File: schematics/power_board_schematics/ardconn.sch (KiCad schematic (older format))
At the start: 1 part, among them J7 CONN_01X16

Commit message: Added more connections
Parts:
- added J8: Conn_01x08_Male, symbol Connector:Conn_01x08_Male
- added U1: Conn_0_to_7, symbol custom:Conn_0_to_7
- added U2: conn_8_to_13, symbol custom:conn_8_to_13
- added U3: Conn_14_to_21, symbol custom:Conn_14_to_21
- added U4: conn_A8_to_A15, symbol custom:conn_A8_to_A15
- added U5: conn_A0_to_A7, symbol custom:conn_A0_to_A7
- added U6: conn_22_to_53, symbol custom:conn_22_to_53
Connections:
- new net Ignition_Primary_Power: U6.28 (Pin_28)
- new net Ignition_Primary_Select: U6.29 (Pin_31)
- new net Ignition_Secondary_Power: U6.37 (Pin_16)
- new net Ignition_Secondary_Select: U6.36 (Pin_36)
- new net Limitsw_Linac_EXT: U6.31 (Pin_31)
- new net Limitsw_Linac_Ret: U6.30 (Pin_30)
- new net Limitsw_Remotefill_CLS: U6.35 (Pin_14)
- new net Limitsw_Remotefill_OPN: U6.34 (Pin_34)
- new net Limitsw_Remotevent_OPN: U6.33 (Pin_12)
- new net Limitsw_Removevent_CLS: U6.32 (Pin_32)
- new net Linactuator_Power: U6.22 (Pin_22)
- new net Linactuator_Select: U6.23 (Pin_31)
- new net Remotefill_Power: U6.26 (Pin_26)
- new net Remotefill_Select: U6.27 (Pin_31)
- new net Remotevent_Power: U6.25 (Pin_31)
- new net Remotevent_Select: U6.24 (Pin_24)
- new net SD_SS: U6.53 (Pin_32)
- new net Sevenseg_A: U6.39 (Pin_18)
- new net Sevenseg_B: U6.40 (Pin_40)
- new net Sevenseg_C: U6.43 (Pin_22)
- new net Sevenseg_D: U6.45 (Pin_24)
- new net Sevenseg_D1: U6.47 (Pin_26)
- new net Sevenseg_D2: U6.46 (Pin_46)
- new net Sevenseg_DP: U6.44 (Pin_44)
- new net Sevenseg_E: U6.42 (Pin_42)
- new net Sevenseg_F: U6.41 (Pin_20)
- new net Sevenseg_G: U6.38 (Pin_38)
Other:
- note added: "Arduino Pins 14 - 21"
- note added: "Arduino Pins 22 - 53"
- note added: "Arduino Pins 8 - 13 \n+ some others\n"
- note added: "Arduino Pins A0 - A7"
- note added: "Arduino Pins A8 - A15"
- note added: "Arduino Pins Power"
- note added: "Arudino Pins 0 - 7"
- moved on the sheet: J7

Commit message: First commit
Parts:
- removed J8: Conn_01x08_Male, symbol Connector:Conn_01x08_Male
- added Button: SW_Push, symbol Switch:SW_Push
- added U?: conn_power, symbol custom:conn_power
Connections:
- net GND: now reaches U6.56 (Pin_56)
- net GND: now also U6.57 (Pin_57)
- net Ignition_Primary_Power: no longer names the net of U6.28 (Pin_28)
- net Ignition_Primary_Select: no longer names the net of U6.29 (Pin_31)
- net Ignition_Secondary_Power: no longer names the net of U6.37 (Pin_16)
- net Ignition_Secondary_Select: no longer names the net of U6.36 (Pin_36)
- net Limitsw_Linac_EXT: no longer names the net of U6.31 (Pin_31)
- net Limitsw_Linac_Ret: no longer names the net of U6.30 (Pin_30)
- net Limitsw_Remotefill_CLS: no longer names the net of U6.35 (Pin_14)
- net Limitsw_Remotefill_OPN: no longer names the net of U6.34 (Pin_34)
- net Limitsw_Remotevent_OPN: no longer names the net of U6.33 (Pin_12)
- net Limitsw_Removevent_CLS: no longer names the net of U6.32 (Pin_32)
- net Remotefill_Power: no longer names the net of U6.26 (Pin_26)
- net Remotefill_Select: no longer names the net of U6.27 (Pin_31)
- net Remotevent_Power: no longer names the net of U6.25 (Pin_31)
- net Remotevent_Select: no longer names the net of U6.24 (Pin_24)
- new net: Button.1, U?.2 (RESET)
- new net: Button.2, U?.5 (GND)
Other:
- moved on the sheet: U2

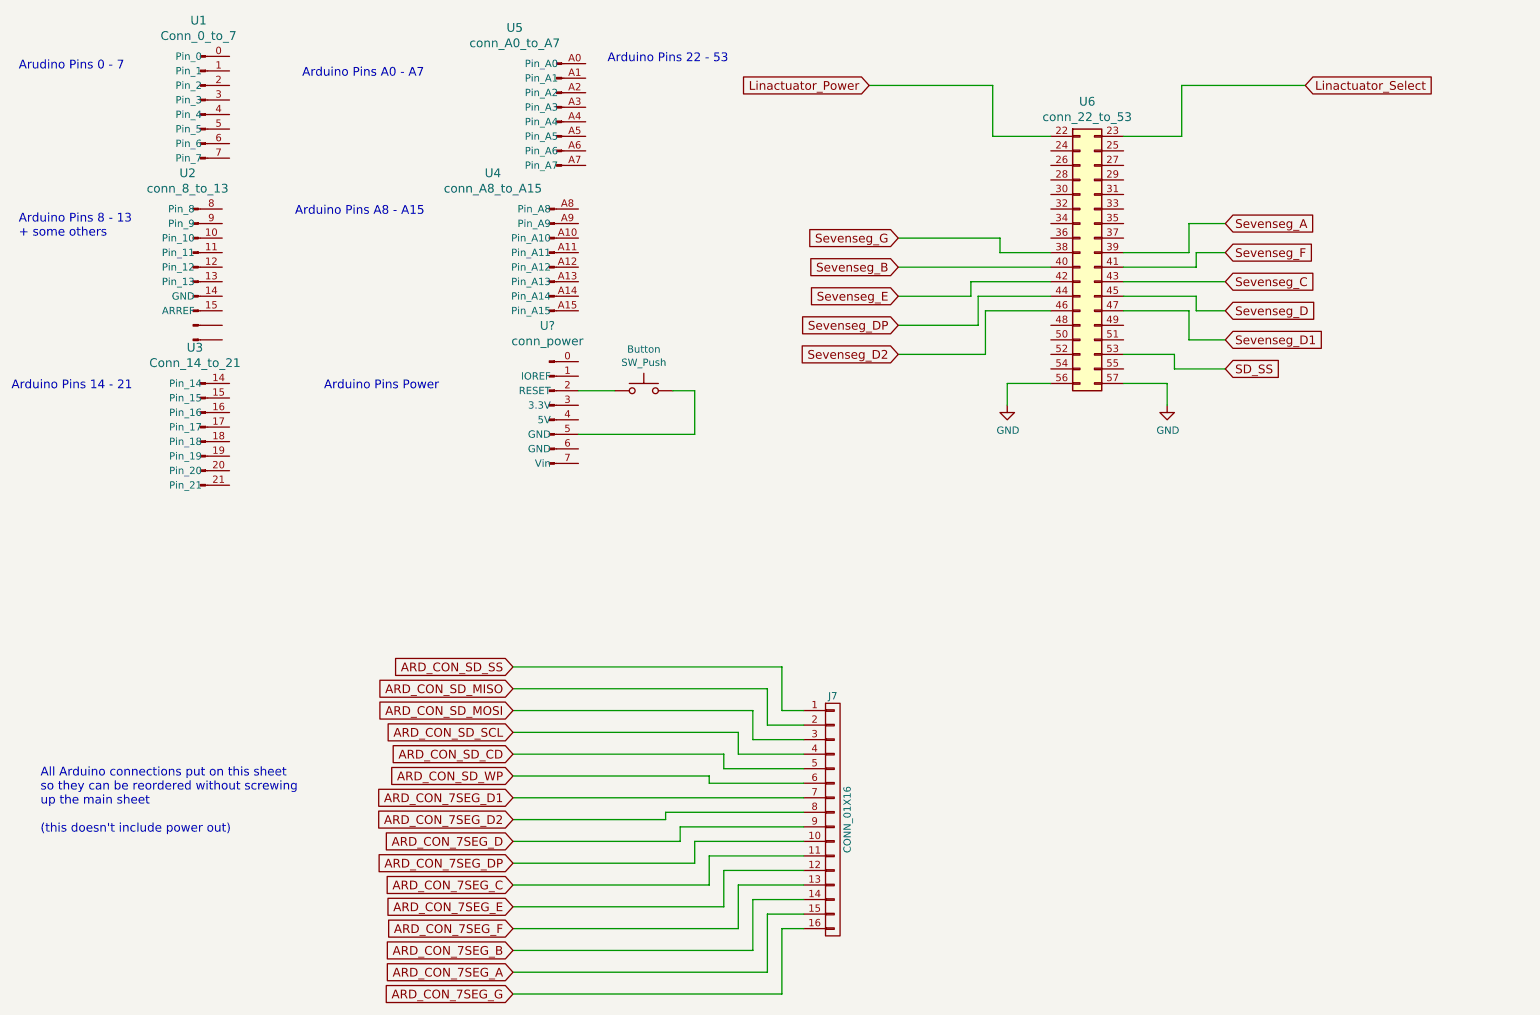
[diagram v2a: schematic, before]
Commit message: Set CD and WP to 54 and 55 respectively
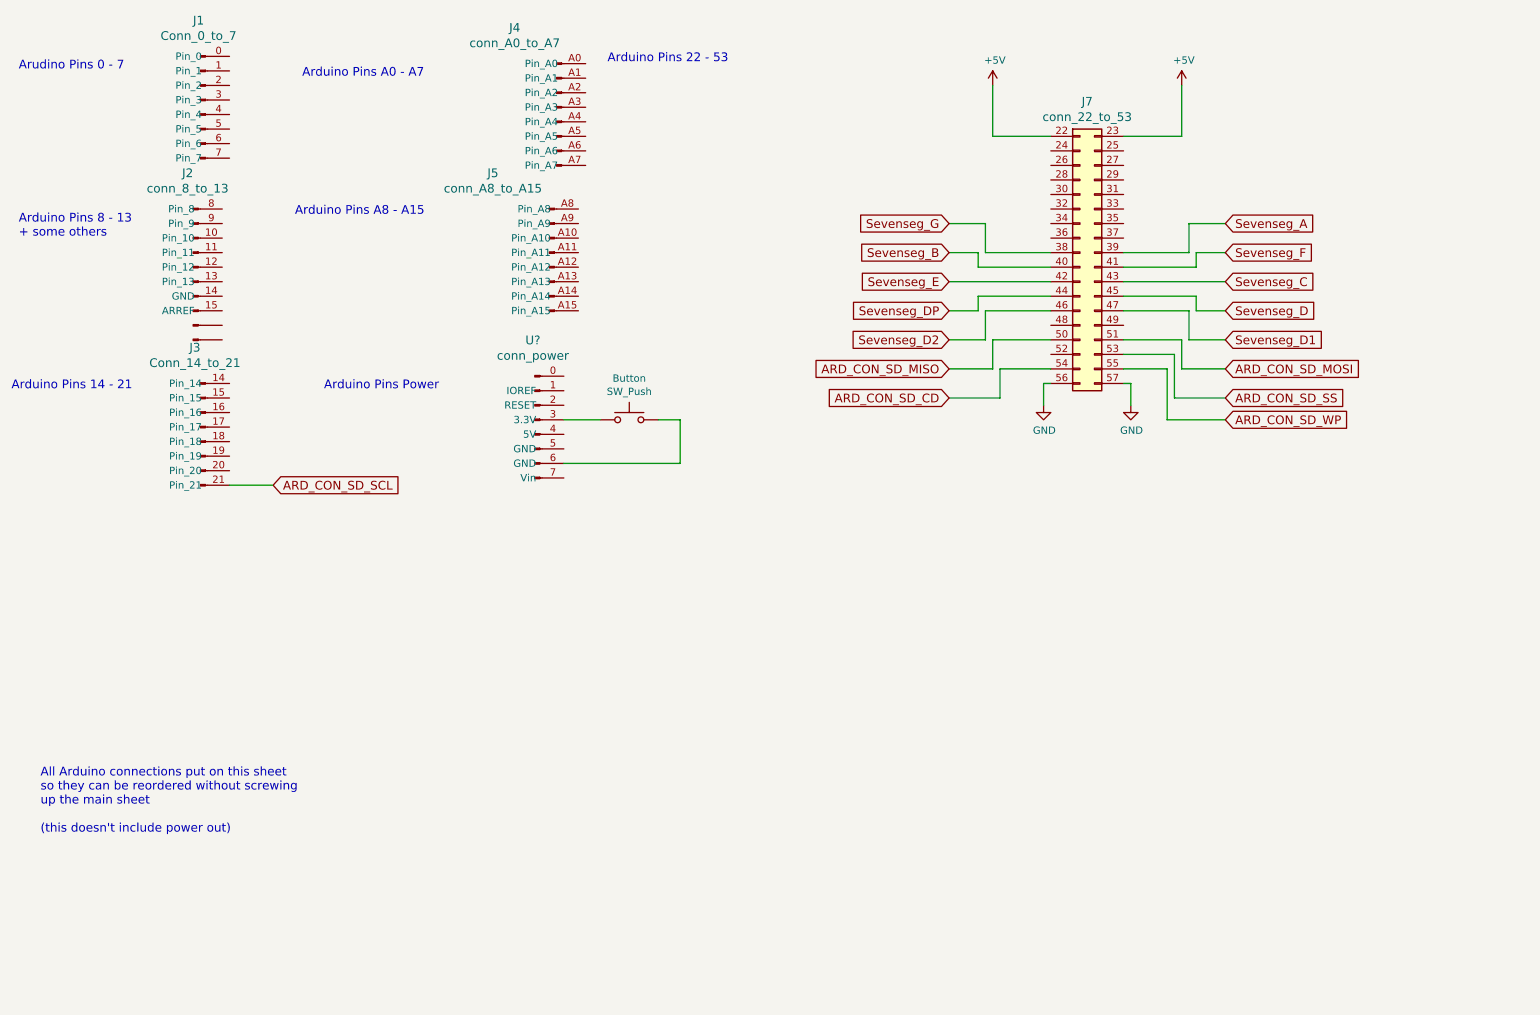
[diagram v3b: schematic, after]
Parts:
- removed J7: CONN_01X16, Pin_Headers:Pin_Header_Straight_2x08_Pitch2.54mm, symbol rlcs_power-rescue:CONN_01X16
- removed U?: conn_power, symbol custom:conn_power
- added U?: conn_power, symbol custom:conn_power
- renumbered U1 to J1, U2 to J2, U3 to J3, U5 to J4, U4 to J5, U6 to J7
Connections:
- net Linactuator_Select is gone; now on net +5V: J7.23 (Pin_31)
- net SD_SS is gone; now on net ARD_CON_SD_SS: J7.53 (Pin_32)
- net ARD_CON_SD_CD: now also J7.54 (Pin_54)
- net ARD_CON_SD_MISO: now also J7.50 (Pin_50)
- net ARD_CON_SD_MOSI: now also J7.51 (Pin_30)
- net ARD_CON_SD_SCL: now also J3.21 (Pin_21)
- net ARD_CON_SD_WP: now also J7.55 (Pin_55)
- net at Button.1: now also U?.3 (3.3V)
- net at Button.2: now also U?.6 (GND)
- net Linactuator_Power renamed +5V
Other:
- moved on the sheet: Button

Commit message: third commit, mainly made it more consistent
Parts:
- gave numbers to parts that had none: 1
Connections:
- net at Button.1: now also J6.2 (RESET); no longer J6.3 (3.3V)
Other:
- moved on the sheet: Button
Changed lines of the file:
@@
 L Switch:SW_Push Button
 U 1 1 5EB5D71A
-P 4900 3350
-F 0 "Button" H 4900 3635 50  0000 C CNN
-F 1 "SW_Push" H 4900 3544 50  0000 C CNN
-F 2 "" H 4900 3550 50  0001 C CNN
-F 3 "~" H 4900 3550 50  0001 C CNN
-	1    4900 3350
+P 4900 3250
+F 0 "Button" H 4900 3535 50  0000 C CNN
+F 1 "SW_Push" H 4900 3444 50  0000 C CNN
+F 2 "" H 4900 3450 50  0001 C CNN
+F 3 "~" H 4900 3450 50  0001 C CNN
+	1    4900 3250
 	1    0    0    -1
 $EndComp
@@
 	5250 3650 4450 3650
 Wire Wire Line
-	4700 3350 4450 3350
+	4700 3250 4450 3250
 Text GLabel 9000 2200 2    60   Input ~ 0
 Sevenseg_F
@@
 Sevenseg_DP
 Wire Wire Line
-	5250 3350 5250 3650
-Wire Wire Line
-	5100 3350 5250 3350
+	5100 3250 5250 3250
 Wire Wire Line
 	8750 2800 9000 2800
@@
 	8600 3000 8300 3000
 $Comp
-L custom:conn_power U?
+L custom:conn_power J6
 U 1 1 5ED49DCC
 P 4350 3000
-F 0 "U?" H 4237 3197 60  0000 C CNN
+F 0 "J6" H 4237 3197 60  0000 C CNN
 F 1 "conn_power" H 4237 3091 60  0000 C CNN
 F 2 "" H 4350 3200 60  0001 C CNN
@@
 	1    0    0    -1
 $EndComp
+Wire Wire Line
+	5250 3250 5250 3650
 $EndSCHEMATC

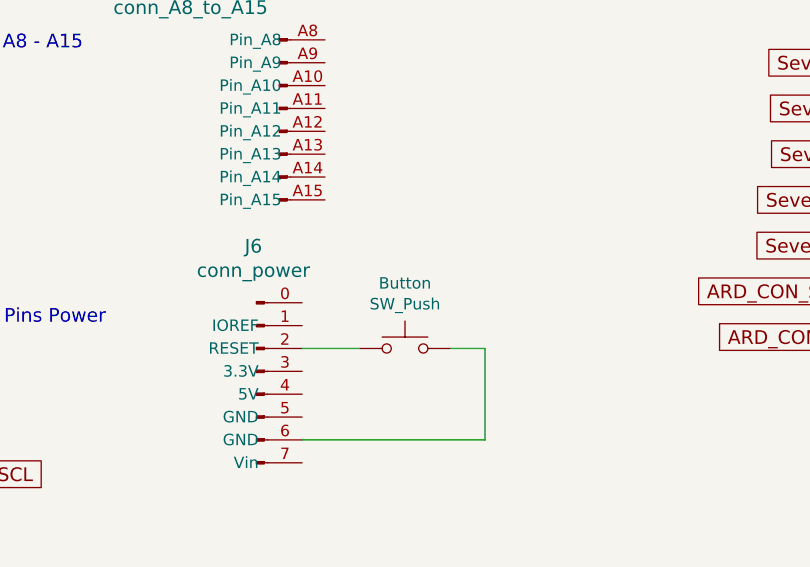
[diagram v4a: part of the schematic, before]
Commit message: Fixed the reference designators
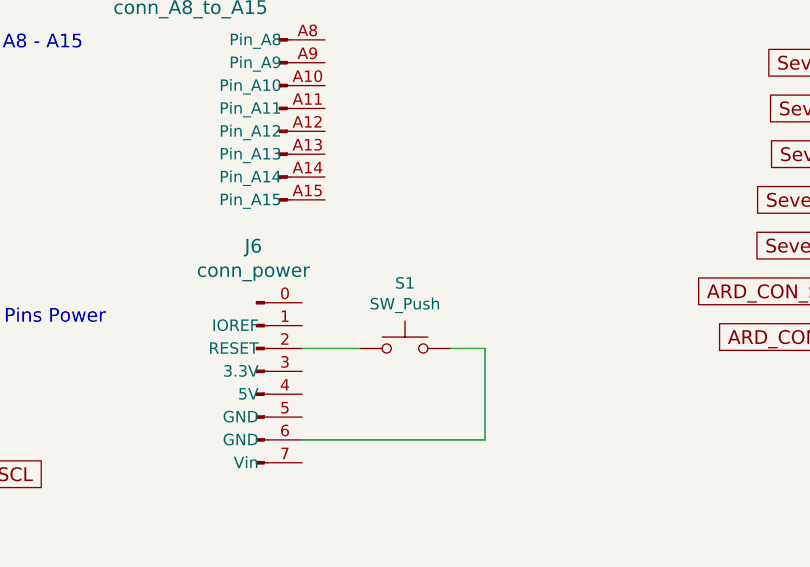
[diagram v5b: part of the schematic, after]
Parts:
- renumbered Button to S1
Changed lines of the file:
@@
 	8700 1400 8700 1050
 $Comp
-L Switch:SW_Push Button
+L Switch:SW_Push S1
 U 1 1 5EB5D71A
 P 4900 3250
-F 0 "Button" H 4900 3535 50  0000 C CNN
+F 0 "S1" H 4900 3535 50  0000 C CNN
 F 1 "SW_Push" H 4900 3444 50  0000 C CNN
 F 2 "" H 4900 3450 50  0001 C CNN

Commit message: Made the pcb
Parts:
- J10: renamed from J3; footprint (none) -> Connector_PinSocket_2.54mm:PinSocket_1x08_P2.54mm_Vertical
- J11: renamed from J6; footprint (none) -> Connector_PinSocket_2.54mm:PinSocket_1x08_P2.54mm_Vertical
- J12: renamed from J5; footprint (none) -> Connector_PinSocket_2.54mm:PinSocket_1x08_P2.54mm_Vertical
- J13: renamed from J4; footprint (none) -> Connector_PinSocket_2.54mm:PinSocket_1x08_P2.54mm_Vertical
- J14: renamed from J7; footprint (none) -> Connector_PinSocket_2.54mm:PinSocket_2x18_P2.54mm_Vertical
- J8: renamed from J1; footprint (none) -> Connector_PinSocket_2.54mm:PinSocket_1x08_P2.54mm_Vertical
- J9: renamed from J2; footprint (none) -> Connector_PinHeader_2.54mm:PinHeader_1x10_P2.54mm_Vertical
- S1: footprint (none) -> Button_Switch_SMD:SW_DIP_SPSTx01_Slide_9.78x4.72mm_W8.61mm_P2.54mm
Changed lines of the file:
@@
 ARD_CON_SD_SCL
 $Comp
-L custom:conn_22_to_53 J7
+L custom:conn_22_to_53 J14
 U 1 1 5E7AFC08
 P 8050 2200
-F 0 "J7" H 8050 3239 60  0000 C CNN
+F 0 "J14" H 8050 3239 60  0000 C CNN
 F 1 "conn_22_to_53" H 8050 3133 60  0000 C CNN
-F 2 "" H 8000 3250 60  0001 C CNN
+F 2 "Connector_PinSocket_2.54mm:PinSocket_2x18_P2.54mm_Vertical" H 8000 3250 60  0001 C CNN
 F 3 "" H 8000 3250 60  0001 C CNN
 	1    8050 2200
@@
 $EndComp
 $Comp
-L custom:Conn_0_to_7 J1
+L custom:Conn_0_to_7 J8
 U 1 1 5E7B26E9
 P 2000 1100
-F 0 "J1" H 1937 1597 60  0000 C CNN
+F 0 "J8" H 1937 1597 60  0000 C CNN
 F 1 "Conn_0_to_7" H 1937 1491 60  0000 C CNN
-F 2 "" H 1900 1800 60  0001 C CNN
+F 2 "Connector_PinSocket_2.54mm:PinSocket_1x08_P2.54mm_Vertical" H 1900 1800 60  0001 C CNN
 F 3 "" H 1900 1800 60  0001 C CNN
 	1    2000 1100
@@
 $EndComp
 $Comp
-L custom:conn_8_to_13 J2
+L custom:conn_8_to_13 J9
 U 1 1 5E7B5F51
 P 2000 2250
-F 0 "J2" H 1862 2847 60  0000 C CNN
+F 0 "J9" H 1862 2847 60  0000 C CNN
 F 1 "conn_8_to_13" H 1862 2741 60  0000 C CNN
-F 2 "" H 2000 3150 60  0001 C CNN
+F 2 "Connector_PinHeader_2.54mm:PinHeader_1x10_P2.54mm_Vertical" H 2000 3150 60  0001 C CNN
 F 3 "" H 2000 3150 60  0001 C CNN
 	1    2000 2250
@@
 $EndComp
 $Comp
-L custom:Conn_14_to_21 J3
+L custom:Conn_14_to_21 J10
 U 1 1 5E7B8C25
 P 2050 3350
-F 0 "J3" H 1912 3847 60  0000 C CNN
+F 0 "J10" H 1912 3847 60  0000 C CNN
 F 1 "Conn_14_to_21" H 1912 3741 60  0000 C CNN
-F 2 "" H 1950 4250 60  0001 C CNN
+F 2 "Connector_PinSocket_2.54mm:PinSocket_1x08_P2.54mm_Vertical" H 1950 4250 60  0001 C CNN
 F 3 "" H 1950 4250 60  0001 C CNN
 	1    2050 3350
@@
 $EndComp
 $Comp
-L custom:conn_A0_to_A7 J4
+L custom:conn_A0_to_A7 J13
 U 1 1 5E7C0D80
 P 4500 1250
-F 0 "J4" H 4112 1847 60  0000 C CNN
+F 0 "J13" H 4112 1847 60  0000 C CNN
 F 1 "conn_A0_to_A7" H 4112 1741 60  0000 C CNN
-F 2 "" H 4500 1850 60  0001 C CNN
+F 2 "Connector_PinSocket_2.54mm:PinSocket_1x08_P2.54mm_Vertical" H 4500 1850 60  0001 C CNN
 F 3 "" H 4500 1850 60  0001 C CNN
 	1    4500 1250
@@
 $EndComp
 $Comp
-L custom:conn_A8_to_A15 J5
+L custom:conn_A8_to_A15 J12
 U 1 1 5E7C1AAF
 P 4400 2250
-F 0 "J5" H 3962 2847 60  0000 C CNN
+F 0 "J12" H 3962 2847 60  0000 C CNN
 F 1 "conn_A8_to_A15" H 3962 2741 60  0000 C CNN
-F 2 "" H 4450 2850 60  0001 C CNN
+F 2 "Connector_PinSocket_2.54mm:PinSocket_1x08_P2.54mm_Vertical" H 4450 2850 60  0001 C CNN
 F 3 "" H 4450 2850 60  0001 C CNN
 	1    4400 2250
@@
 F 0 "S1" H 4900 3535 50  0000 C CNN
 F 1 "SW_Push" H 4900 3444 50  0000 C CNN
-F 2 "" H 4900 3450 50  0001 C CNN
+F 2 "Button_Switch_SMD:SW_DIP_SPSTx01_Slide_9.78x4.72mm_W8.61mm_P2.54mm" H 4900 3450 50  0001 C CNN
 F 3 "~" H 4900 3450 50  0001 C CNN
 	1    4900 3250
@@
 	8750 2800 9000 2800
 $Comp
-L power:GND #PWR?
+L power:GND #PWR027
 U 1 1 5EBCBE4C
 P 7750 3250
-F 0 "#PWR?" H 7750 3000 50  0001 C CNN
+F 0 "#PWR027" H 7750 3000 50  0001 C CNN
 F 1 "GND" H 7755 3077 50  0000 C CNN
 F 2 "" H 7750 3250 50  0001 C CNN
@@
 	7750 3100 7750 3250
 $Comp
-L power:GND #PWR?
+L power:GND #PWR028
 U 1 1 5EBD1205
 P 8350 3250
-F 0 "#PWR?" H 8350 3000 50  0001 C CNN
+F 0 "#PWR028" H 8350 3000 50  0001 C CNN
 F 1 "GND" H 8355 3077 50  0000 C CNN
 F 2 "" H 8350 3250 50  0001 C CNN
@@
 	8350 3100 8350 3250
 $Comp
-L power:+5V #PWR?
+L power:+5V #PWR026
 U 1 1 5ECC7808
 P 7400 1050
-F 0 "#PWR?" H 7400 900 50  0001 C CNN
+F 0 "#PWR026" H 7400 900 50  0001 C CNN
 F 1 "+5V" H 7415 1223 50  0000 C CNN
 F 2 "" H 7400 1050 50  0001 C CNN
@@
 $EndComp
 $Comp
-L power:+5V #PWR?
+L power:+5V #PWR029
 U 1 1 5ECC83F1
 P 8700 1050
-F 0 "#PWR?" H 8700 900 50  0001 C CNN
+F 0 "#PWR029" H 8700 900 50  0001 C CNN
 F 1 "+5V" H 8715 1223 50  0000 C CNN
 F 2 "" H 8700 1050 50  0001 C CNN
@@
 	8600 3000 8300 3000
 $Comp
-L custom:conn_power J6
+L custom:conn_power J11
 U 1 1 5ED49DCC
 P 4350 3000
-F 0 "J6" H 4237 3197 60  0000 C CNN
+F 0 "J11" H 4237 3197 60  0000 C CNN
 F 1 "conn_power" H 4237 3091 60  0000 C CNN
-F 2 "" H 4350 3200 60  0001 C CNN
+F 2 "Connector_PinSocket_2.54mm:PinSocket_1x08_P2.54mm_Vertical" H 4350 3200 60  0001 C CNN
 F 3 "" H 4350 3200 60  0001 C CNN
 	1    4350 3000

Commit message: Updated pcb
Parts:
- J9: footprint Connector_PinHeader_2.54mm:PinHeader_1x10_P2.54mm_Vertical -> Connector_PinSocket_2.54mm:PinSocket_1x10_P2.54mm_Vertical
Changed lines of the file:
@@
 F 0 "J9" H 1862 2847 60  0000 C CNN
 F 1 "conn_8_to_13" H 1862 2741 60  0000 C CNN
-F 2 "Connector_PinHeader_2.54mm:PinHeader_1x10_P2.54mm_Vertical" H 2000 3150 60  0001 C CNN
+F 2 "Connector_PinSocket_2.54mm:PinSocket_1x10_P2.54mm_Vertical" H 2000 3150 60  0001 C CNN
 F 3 "" H 2000 3150 60  0001 C CNN
 	1    2000 2250

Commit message: Updated PCB, still need to edit traces
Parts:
- S1: footprint Button_Switch_SMD:SW_DIP_SPSTx01_Slide_9.78x4.72mm_W8.61mm_P2.54mm -> Button_Switch_SMD:SW_Push_SPST_NO_Alps_SKRK
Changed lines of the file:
@@
 F 0 "S1" H 4900 3535 50  0000 C CNN
 F 1 "SW_Push" H 4900 3444 50  0000 C CNN
-F 2 "Button_Switch_SMD:SW_DIP_SPSTx01_Slide_9.78x4.72mm_W8.61mm_P2.54mm" H 4900 3450 50  0001 C CNN
+F 2 "Button_Switch_SMD:SW_Push_SPST_NO_Alps_SKRK" H 4900 3450 50  0001 C CNN
 F 3 "~" H 4900 3450 50  0001 C CNN
 	1    4900 3250
